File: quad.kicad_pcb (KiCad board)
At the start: 2 copper layers, 21 parts, among them M0 Fan, M1 Fan, M2 Fan, M3 Fan, Q0 Si2318DS, Q1 Si2318DS, Q2 Si2318DS, Q4 Si2318DS, U1 LK112M18TR, U2 ICM-20602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

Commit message: Good board outline
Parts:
- removed XTAL1: 16Mhz, Crystal:Crystal_SMD_3225-4Pin_3.2x2.5mm
- added Y1: Crystal_GND24_Small, Crystal:Crystal_SMD_3225-4Pin_3.2x2.5mm, F.Cu at (224.7, 133.0)
- moved Q4 144.6 mm to (229.6, 131.5), turned to 0 degrees
- moved M3 142.4 mm to (220.1, 132.8)
- moved AE1 138.0 mm to (228.2, 137.9)
- moved CX1 133.2 mm to (218.6, 142.8), turned to 0 degrees
- moved CRF1 130.3 mm to (229.3, 135.1), turned to 0 degrees
- moved Q2 124.8 mm to (224.3, 137.5), turned to 0 degrees
- moved CX2 121.5 mm to (204.3, 143.3), turned to 0 degrees
- moved Q0 120.8 mm to (219.4, 139.1), turned to 0 degrees
- moved U1 118.7 mm to (214.0, 140.6), turned to 0 degrees
- moved B1 117.9 mm to (213.5, 129.6)
- moved M0 117.7 mm to (220.1, 126.7)
- moved CRF2 116.5 mm to (208.5, 143.3), turned to 0 degrees
- moved JP1 113.4 mm to (214.4, 136.2)
- moved M2 108.9 mm to (209.5, 138.0), turned to 0 degrees
- moved C1 102.7 mm to (202.6, 138.9), turned to 0 degrees
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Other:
- board outline added: 112 x 112 mm
- rule trace_min: 0.2 -> 0.1524
- rule via_min_drill: 0.3 -> 0.254
- rule via_min_size: 0.4 -> 0.254

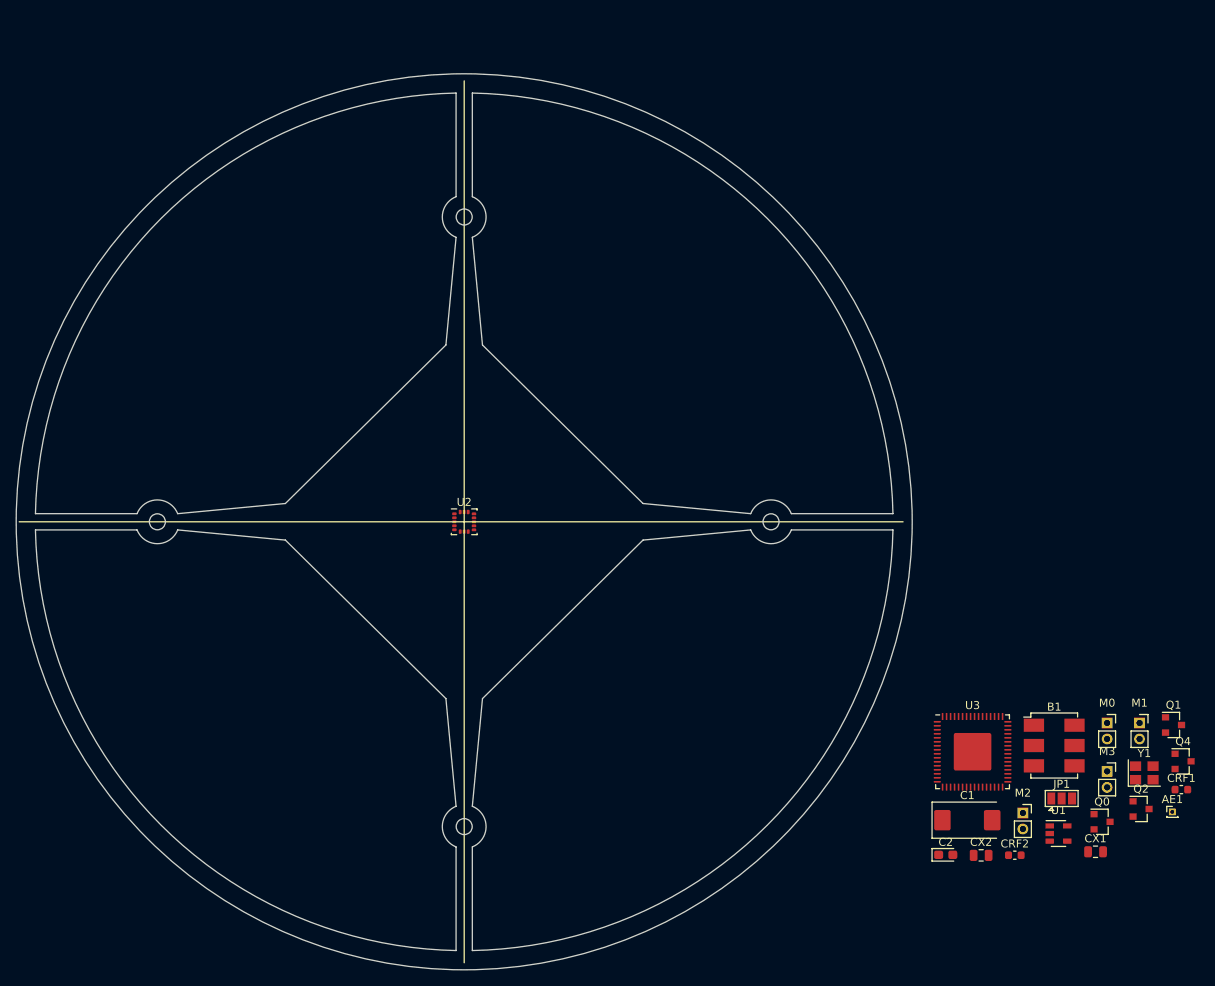
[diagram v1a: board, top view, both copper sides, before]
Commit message: More board layout
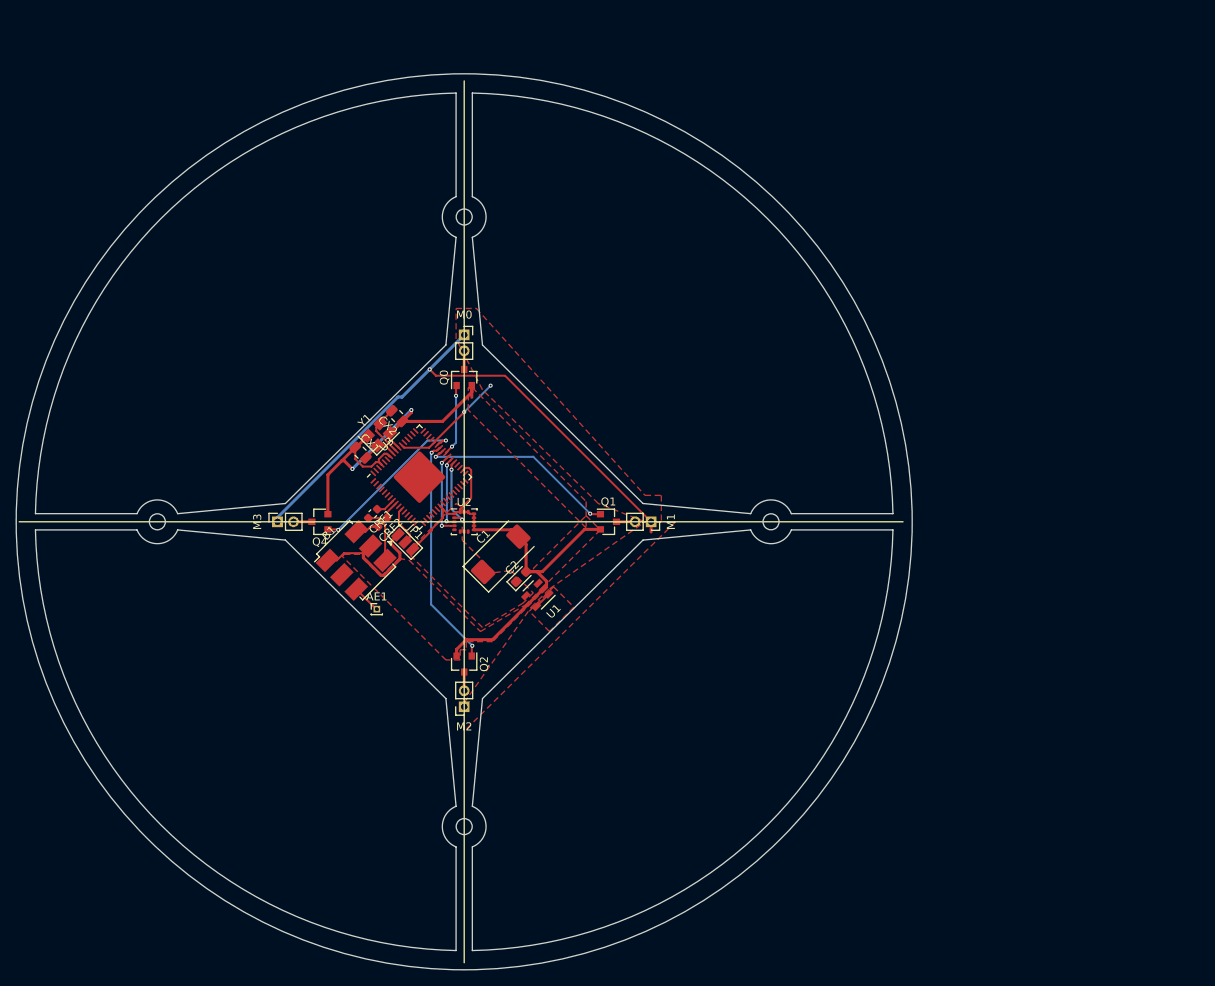
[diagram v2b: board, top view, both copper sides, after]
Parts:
- moved Q4 112.0 mm to (121.7, 101.6), turned to 180 degrees
- moved M3 108.3 mm to (116.4, 101.6), turned to 90 degrees
- moved CRF1 106.8 mm to (128.3, 100.6), turned to 225 degrees
- moved Y1 104.6 mm to (129.0, 90.7), turned to 45 degrees
- moved CX1 104.5 mm to (126.7, 93.0), turned to 315 degrees
- moved AE1 102.6 mm to (128.8, 112.5)
- moved Q0 97.2 mm to (139.7, 83.6), turned to 90 degrees
- moved M0 93.9 mm to (139.7, 78.2)
- moved CX2 91.3 mm to (131.3, 88.4), turned to 135 degrees
- moved B1 90.3 mm to (126.2, 106.4), turned to 45 degrees
- moved CRF2 89.3 mm to (129.5, 101.6), turned to 225 degrees
- moved JP1 88.1 mm to (132.3, 104.1), turned to 315 degrees
- moved Q2 86.5 mm to (139.7, 119.4), turned to 270 degrees
- moved U3 77.2 mm to (134.1, 96.0), turned to 45 degrees
- moved Q1 75.1 mm to (157.7, 101.6)
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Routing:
- net -BATT: track 0.00 -> 112.5 mm, vias 0 -> 2
- net +BATT: track 0.00 -> 72.4 mm, vias 0 -> 1
- net VDD: track 0.00 -> 31.7 mm, vias 0 -> 2
- net M2: track 0.00 -> 28.9 mm, vias 0 -> 2
- net M1: track 0.00 -> 24.8 mm, vias 0 -> 2
- net M3: track 0.00 -> 20.7 mm, vias 0 -> 2
- net MISO: track 0.00 -> 10.3 mm, vias 0 -> 2
- net M0: track 0.00 -> 9.06 mm, vias 0 -> 2
- net MOSI: track 0.00 -> 9.03 mm, vias 0 -> 2
- net SCLK: track 0.00 -> 8.99 mm, vias 0 -> 2
- net Net-(B1-Pad4): track 0.00 -> 6.89 mm
- net Net-(CX2-Pad2): track 0.00 -> 6.81 mm
- net Net-(JP1-Pad2): track 0.00 -> 5.03 mm
- net Net-(CX1-Pad2): track 0.00 -> 4.55 mm
- net Net-(AE1-Pad1): track 0.00 -> 3.61 mm
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- added copper zone on F.Cu, net +BATT
- added copper zone on F.Cu, net -BATT
- added copper zone on F.Cu, net VDD
